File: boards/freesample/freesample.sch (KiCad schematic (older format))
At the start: 5 parts, among them J1 SMA, J2 CONN_3_PWROUT

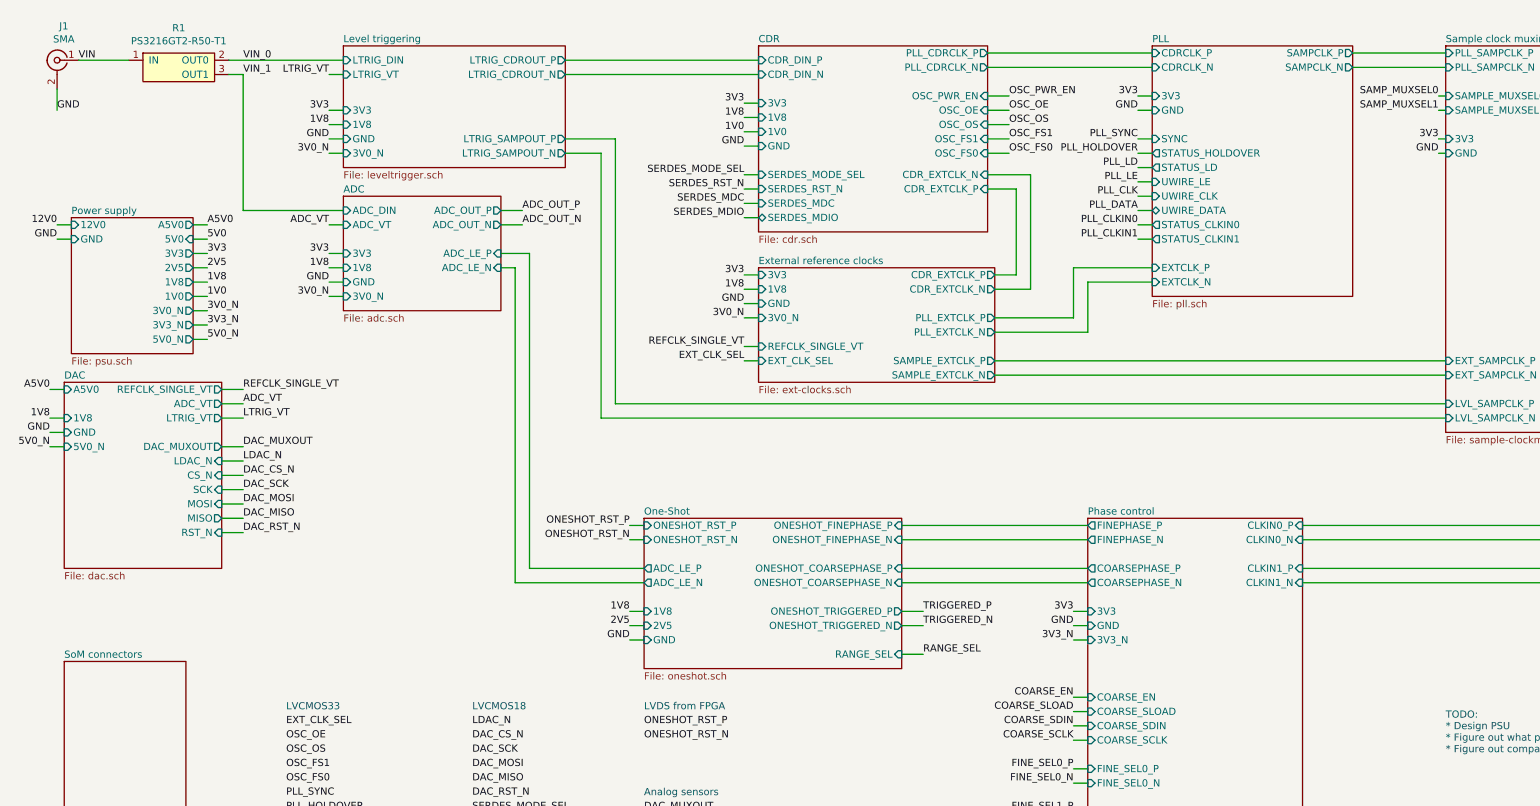
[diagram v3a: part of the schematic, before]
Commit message: Hooked up new power rails
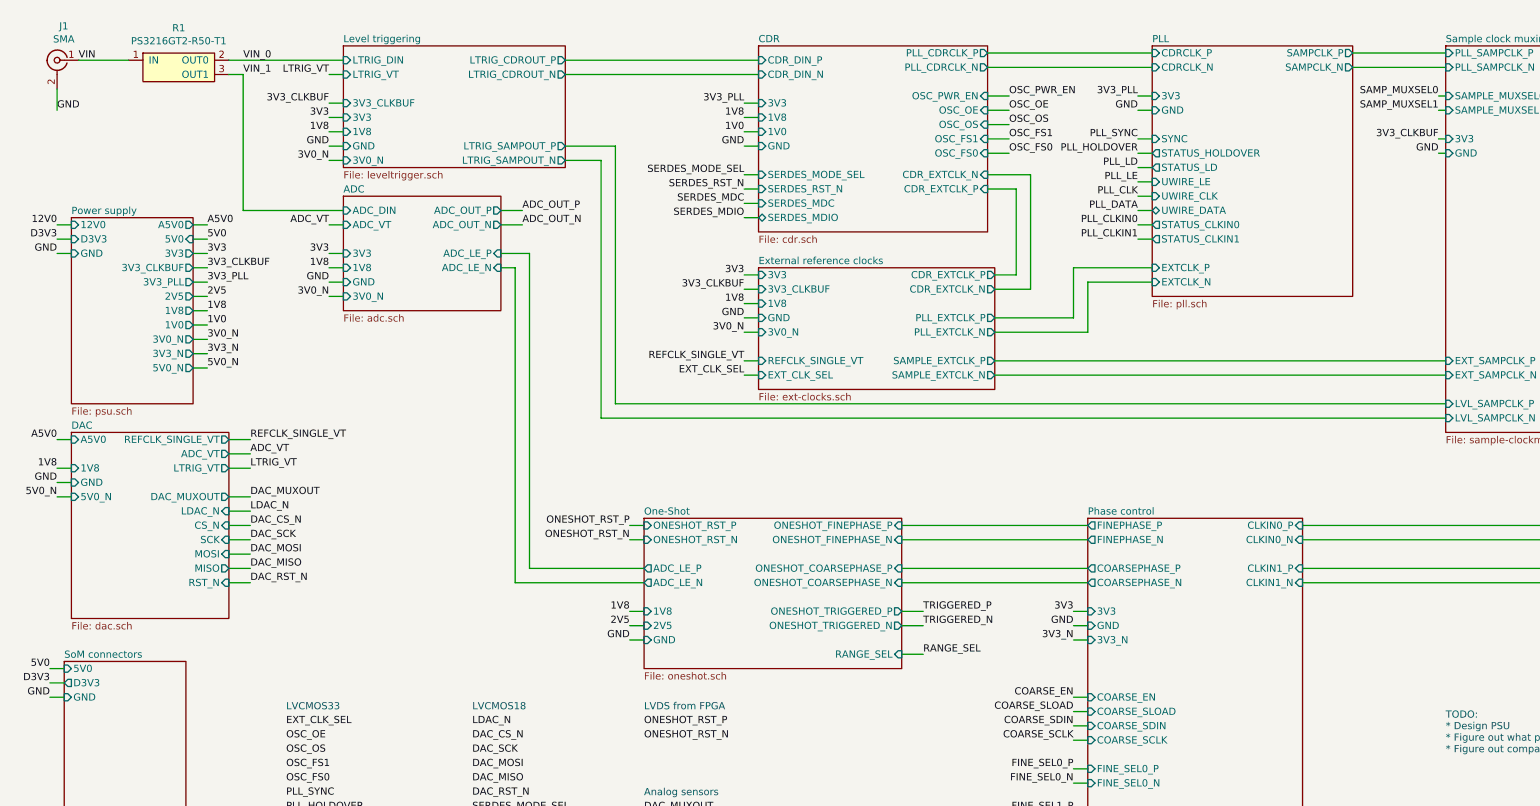
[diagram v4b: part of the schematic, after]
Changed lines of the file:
@@
 Sheet 1 12
 Title "FREESAMPLE Oscilloscope"
-Date "2019-02-23"
+Date "2019-02-26"
 Rev "0.1"
 Comp "Andrew D. Zonenberg / Antikernel Labs"
@@
 $EndDescr
 $Sheet
-S 5650 2300 1650 800
+S 5650 2300 1650 850
 U 5C0E404A
 F0 "External reference clocks" 50
 F1 "ext-clocks.sch" 50
 F2 "3V3" I L 5650 2350 50
-F3 "GND" I L 5650 2550 50
-F4 "3V0_N" I L 5650 2650 50
-F5 "1V8" I L 5650 2450 50
-F6 "REFCLK_SINGLE_VT" I L 5650 2850 50
-F7 "EXT_CLK_SEL" I L 5650 2950 50
+F3 "GND" I L 5650 2650 50
+F4 "3V0_N" I L 5650 2750 50
+F5 "1V8" I L 5650 2550 50
+F6 "REFCLK_SINGLE_VT" I L 5650 2950 50
+F7 "EXT_CLK_SEL" I L 5650 3050 50
 F8 "PLL_EXTCLK_P" O R 7300 2650 50
 F9 "PLL_EXTCLK_N" O R 7300 2750 50
@@
 F12 "CDR_EXTCLK_P" O R 7300 2350 50
 F13 "CDR_EXTCLK_N" O R 7300 2450 50
-$EndSheet
-$Sheet
-S 800  3100 1100 1300
+F14 "3V3_CLKBUF" I L 5650 2450 50
+$EndSheet
+$Sheet
+S 850  3450 1100 1300
 U 5C157454
 F0 "DAC" 50
 F1 "dac.sch" 50
-F2 "LTRIG_VT" O R 1900 3350 50
-F3 "REFCLK_SINGLE_VT" O R 1900 3150 50
-F4 "ADC_VT" O R 1900 3250 50
-F5 "5V0_N" I L 800 3550 50
-F6 "GND" I L 800 3450 50
-F7 "DAC_MUXOUT" O R 1900 3550 50
-F8 "LDAC_N" I R 1900 3650 50
-F9 "CS_N" I R 1900 3750 50
-F10 "SCK" I R 1900 3850 50
-F11 "MOSI" I R 1900 3950 50
-F12 "MISO" O R 1900 4050 50
-F13 "1V8" I L 800 3350 50
-F14 "RST_N" I R 1900 4150 50
-F15 "A5V0" I L 800 3150 50
+F2 "LTRIG_VT" O R 1950 3700 50
+F3 "REFCLK_SINGLE_VT" O R 1950 3500 50
+F4 "ADC_VT" O R 1950 3600 50
+F5 "5V0_N" I L 850 3900 50
+F6 "GND" I L 850 3800 50
+F7 "DAC_MUXOUT" O R 1950 3900 50
+F8 "LDAC_N" I R 1950 4000 50
+F9 "CS_N" I R 1950 4100 50
+F10 "SCK" I R 1950 4200 50
+F11 "MOSI" I R 1950 4300 50
+F12 "MISO" O R 1950 4400 50
+F13 "1V8" I L 850 3700 50
+F14 "RST_N" I R 1950 4500 50
+F15 "A5V0" I L 850 3500 50
 $EndSheet
 $Sheet
@@
 F1 "leveltrigger.sch" 50
 F2 "LTRIG_DIN" I L 2750 850 50
-F3 "3V3" I L 2750 1200 50
-F4 "3V0_N" I L 2750 1500 50
-F5 "GND" I L 2750 1400 50
-F6 "1V8" I L 2750 1300 50
+F3 "3V3" I L 2750 1250 50
+F4 "3V0_N" I L 2750 1550 50
+F5 "GND" I L 2750 1450 50
+F6 "1V8" I L 2750 1350 50
 F7 "LTRIG_VT" I L 2750 950 50
 F8 "LTRIG_CDROUT_P" O R 4300 850 50
 F9 "LTRIG_CDROUT_N" O R 4300 950 50
-F10 "LTRIG_SAMPOUT_P" O R 4300 1400 50
-F11 "LTRIG_SAMPOUT_N" O R 4300 1500 50
+F10 "LTRIG_SAMPOUT_P" O R 4300 1450 50
+F11 "LTRIG_SAMPOUT_N" O R 4300 1550 50
+F12 "3V3_CLKBUF" I L 2750 1150 50
 $EndSheet
 Text Label 5550 1250 2    50   ~ 0
@@
 Wire Wire Line
 	1950 850  2750 850
-Text Label 2650 1200 2    50   ~ 0
+Text Label 2650 1250 2    50   ~ 0
 3V3
 Wire Wire Line
-	2650 1200 2750 1200
-Text Label 2650 1300 2    50   ~ 0
+	2650 1250 2750 1250
+Text Label 2650 1350 2    50   ~ 0
 1V8
-Text Label 2650 1400 2    50   ~ 0
-GND
-Text Label 2650 1500 2    50   ~ 0
+Text Label 2650 1450 2    50   ~ 0
+GND
+Text Label 2650 1550 2    50   ~ 0
 3V0_N
 Wire Wire Line
-	2650 1500 2750 1500
-Wire Wire Line
-	2750 1400 2650 1400
-Wire Wire Line
-	2650 1300 2750 1300
+	2650 1550 2750 1550
+Wire Wire Line
+	2750 1450 2650 1450
+Wire Wire Line
+	2650 1350 2750 1350
 Text Label 2050 850  0    50   ~ 0
 VIN_0
@@
 F0 "SoM connectors" 50
 F1 "som.sch" 50
-$EndSheet
-$Sheet
-S 850  1950 850  950
+F2 "5V0" I L 800 5100 50
+F3 "GND" I L 800 5300 50
+F4 "D3V3" O L 800 5200 50
+$EndSheet
+$Sheet
+S 850  1950 850  1300
 U 5C204CCA
 F0 "Power supply" 50
@@
 F2 "5V0" I R 1700 2100 50
 F3 "3V3" O R 1700 2200 50
-F4 "3V0_N" O R 1700 2600 50
-F5 "1V8" O R 1700 2400 50
-F6 "GND" I L 850 2100 50
-F7 "1V0" O R 1700 2500 50
-F8 "5V0_N" O R 1700 2800 50
+F4 "3V0_N" O R 1700 2800 50
+F5 "1V8" O R 1700 2600 50
+F6 "GND" I L 850 2200 50
+F7 "1V0" O R 1700 2700 50
+F8 "5V0_N" O R 1700 3000 50
 F9 "12V0" I L 850 2000 50
-F10 "3V3_N" O R 1700 2700 50
-F11 "2V5" O R 1700 2300 50
+F10 "3V3_N" O R 1700 2900 50
+F11 "2V5" O R 1700 2500 50
 F12 "A5V0" O R 1700 2000 50
+F13 "D3V3" I L 850 2100 50
+F14 "3V3_PLL" O R 1700 2400 50
+F15 "3V3_CLKBUF" O R 1700 2300 50
 $EndSheet
 Text Label 8300 1100 2    50   ~ 0
-3V3
+3V3_PLL
 Wire Wire Line
 	8300 1100 8400 1100
@@
 Wire Wire Line
 	4000 2000 3850 2000
-Text Label 2050 3250 0    50   ~ 0
+Text Label 2100 3600 0    50   ~ 0
 ADC_VT
 Wire Wire Line
-	2050 3250 1900 3250
-Text Label 2050 3150 0    50   ~ 0
+	2100 3600 1950 3600
+Text Label 2100 3500 0    50   ~ 0
 REFCLK_SINGLE_VT
 Wire Wire Line
-	2050 3150 1900 3150
-Text Label 2050 3350 0    50   ~ 0
+	2100 3500 1950 3500
+Text Label 2100 3700 0    50   ~ 0
 LTRIG_VT
 Wire Wire Line
-	2050 3350 1900 3350
-Text Label 700  3150 2    50   ~ 0
+	2100 3700 1950 3700
+Text Label 750  3500 2    50   ~ 0
 A5V0
 Wire Wire Line
-	700  3150 800  3150
-Text Label 700  3450 2    50   ~ 0
-GND
-Wire Wire Line
-	700  3450 800  3450
-Text Label 700  3550 2    50   ~ 0
+	750  3500 850  3500
+Text Label 750  3800 2    50   ~ 0
+GND
+Wire Wire Line
+	750  3800 850  3800
+Text Label 750  3900 2    50   ~ 0
 5V0_N
 Wire Wire Line
-	700  3550 800  3550
+	750  3900 850  3900
 Text Label 5550 2350 2    50   ~ 0
 3V3
 Wire Wire Line
 	5650 2350 5550 2350
-Text Label 5550 2450 2    50   ~ 0
+Text Label 5550 2550 2    50   ~ 0
 1V8
-Wire Wire Line
-	5550 2450 5650 2450
-Text Label 5550 2550 2    50   ~ 0
-GND
 Wire Wire Line
 	5550 2550 5650 2550
 Text Label 5550 2650 2    50   ~ 0
+GND
+Wire Wire Line
+	5550 2650 5650 2650
+Text Label 5550 2750 2    50   ~ 0
 3V0_N
 Wire Wire Line
-	5550 2650 5650 2650
-Text Label 5550 2850 2    50   ~ 0
+	5550 2750 5650 2750
+Text Label 5550 2950 2    50   ~ 0
 REFCLK_SINGLE_VT
 Wire Wire Line
-	5550 2850 5650 2850
-Text Label 5550 2950 2    50   ~ 0
+	5550 2950 5650 2950
+Text Label 5550 3050 2    50   ~ 0
 EXT_CLK_SEL
 Wire Wire Line
-	5550 2950 5650 2950
+	5550 3050 5650 3050
 $Sheet
 S 10450 750  1900 2700
@@
 Text Label 3650 6000 0    50   ~ 0
 DAC_RST_N
-Text Label 2050 3550 0    50   ~ 0
+Text Label 2100 3900 0    50   ~ 0
 DAC_MUXOUT
-Text Label 2050 3650 0    50   ~ 0
+Text Label 2100 4000 0    50   ~ 0
 LDAC_N
-Text Label 2050 3750 0    50   ~ 0
+Text Label 2100 4100 0    50   ~ 0
 DAC_CS_N
-Text Label 2050 3850 0    50   ~ 0
+Text Label 2100 4200 0    50   ~ 0
 DAC_SCK
-Text Label 2050 3950 0    50   ~ 0
+Text Label 2100 4300 0    50   ~ 0
 DAC_MOSI
-Text Label 2050 4050 0    50   ~ 0
+Text Label 2100 4400 0    50   ~ 0
 DAC_MISO
-Text Label 2050 4150 0    50   ~ 0
+Text Label 2100 4500 0    50   ~ 0
 DAC_RST_N
 Wire Wire Line
-	2050 3550 1900 3550
-Wire Wire Line
-	1900 3650 2050 3650
-Wire Wire Line
-	2050 3750 1900 3750
-Wire Wire Line
-	1900 3850 2050 3850
-Wire Wire Line
-	2050 3950 1900 3950
-Wire Wire Line
-	1900 4050 2050 4050
-Wire Wire Line
-	2050 4150 1900 4150
+	2100 3900 1950 3900
+Wire Wire Line
+	1950 4000 2100 4000
+Wire Wire Line
+	2100 4100 1950 4100
+Wire Wire Line
+	1950 4200 2100 4200
+Wire Wire Line
+	2100 4300 1950 4300
+Wire Wire Line
+	1950 4400 2100 4400
+Wire Wire Line
+	2100 4500 1950 4500
 Text Label 5550 1650 2    50   ~ 0
 SERDES_MODE_SEL
@@
 OSC_OE
 Text Label 5550 1150 2    50   ~ 0
-3V3
+3V3_PLL
 Wire Wire Line
 	5550 1150 5650 1150
@@
 	4300 950  5650 950
 Wire Wire Line
-	4300 1500 4550 1500
-Wire Wire Line
-	4550 1500 4550 3350
-Wire Wire Line
 	4550 3350 10450 3350
-Wire Wire Line
-	4300 1400 4650 1400
-Wire Wire Line
-	4650 1400 4650 3250
 Wire Wire Line
 	4650 3250 10450 3250
@@
 	13000 4500 9450 4500
 Text Label 10400 1400 2    50   ~ 0
-3V3
+3V3_CLKBUF
 Wire Wire Line
 	10400 1400 10450 1400
@@
 Text Notes 4850 6000 0    50   ~ 0
 Analog sensors
-Text Label 700  3350 2    50   ~ 0
+Text Label 750  3700 2    50   ~ 0
 1V8
 Wire Wire Line
-	700  3350 800  3350
+	750  3700 850  3700
 Text Notes 3650 5400 0    50   ~ 0
 LVCMOS18
@@
 Wire Wire Line
 	1800 2200 1700 2200
-Text Label 1800 2400 0    50   ~ 0
+Text Label 1800 2600 0    50   ~ 0
 1V8
-Wire Wire Line
-	1800 2400 1700 2400
-Text Label 1800 2500 0    50   ~ 0
-1V0
-Wire Wire Line
-	1800 2500 1700 2500
-Text Label 1800 2600 0    50   ~ 0
-3V0_N
 Wire Wire Line
 	1800 2600 1700 2600
 Text Label 1800 2700 0    50   ~ 0
-3V3_N
+1V0
 Wire Wire Line
 	1800 2700 1700 2700
 Text Label 1800 2800 0    50   ~ 0
+3V0_N
+Wire Wire Line
+	1800 2800 1700 2800
+Text Label 1800 2900 0    50   ~ 0
+3V3_N
+Wire Wire Line
+	1800 2900 1700 2900
+Text Label 1800 3000 0    50   ~ 0
 5V0_N
 Wire Wire Line
-	1800 2800 1700 2800
+	1800 3000 1700 3000
 Text Label 750  2000 2    50   ~ 0
 12V0
 Wire Wire Line
 	750  2000 850  2000
-Text Label 750  2100 2    50   ~ 0
-GND
-Wire Wire Line
-	750  2100 850  2100
+Text Label 750  2200 2    50   ~ 0
+GND
+Wire Wire Line
+	750  2200 850  2200
 NoConn ~ 13100 1000
 Text Label 13200 900  0    50   ~ 0
@@
 Wire Wire Line
 	4750 4800 4850 4800
-Text Label 1800 2300 0    50   ~ 0
+Text Label 1800 2500 0    50   ~ 0
 2V5
 Wire Wire Line
-	1800 2300 1700 2300
+	1800 2500 1700 2500
 Text Notes 10450 5700 0    50   ~ 0
 TODO:\n* Design PSU\n* Figure out what power rails may need filtering\n* Figure out compatibility of all of the differential I/O standards
@@
 Wire Wire Line
 	1800 2000 1700 2000
+Text Label 750  2100 2    50   ~ 0
+D3V3
+Wire Wire Line
+	750  2100 850  2100
+Text Label 700  5100 2    50   ~ 0
+5V0
+Wire Wire Line
+	700  5100 800  5100
+Text Label 700  5200 2    50   ~ 0
+D3V3
+Wire Wire Line
+	700  5200 800  5200
+Text Label 700  5300 2    50   ~ 0
+GND
+Wire Wire Line
+	700  5300 800  5300
+Text Label 1800 2300 0    50   ~ 0
+3V3_CLKBUF
+Wire Wire Line
+	1800 2300 1700 2300
+Text Label 1800 2400 0    50   ~ 0
+3V3_PLL
+Wire Wire Line
+	1800 2400 1700 2400
+Text Label 5550 2450 2    50   ~ 0
+3V3_CLKBUF
+Wire Wire Line
+	5550 2450 5650 2450
+Text Label 2650 1150 2    50   ~ 0
+3V3_CLKBUF
+Wire Wire Line
+	2650 1150 2750 1150
+Wire Wire Line
+	4300 1550 4550 1550
+Wire Wire Line
+	4550 1550 4550 3350
+Wire Wire Line
+	4300 1450 4650 1450
+Wire Wire Line
+	4650 1450 4650 3250
 $EndSCHEMATC

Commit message: Continued PSU design
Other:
- note added: "TODO:\n* Finish PSU\n* Figure out compatibility of all of the differential I/O standards\n and add level shifters/buffers as needed"
- note removed: "TODO:\n* Design PSU\n* Figure out what power rails may need filtering\n* Figure out compatibility of all of the differential I/O standards"
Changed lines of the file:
@@
 	1800 2500 1700 2500
 Text Notes 10450 5700 0    50   ~ 0
-TODO:\n* Design PSU\n* Figure out what power rails may need filtering\n* Figure out compatibility of all of the differential I/O standards
+TODO:\n* Finish PSU\n* Figure out compatibility of all of the differential I/O standards\n  and add level shifters/buffers as needed
 Text Label 1800 2000 0    50   ~ 0
 A5V0
